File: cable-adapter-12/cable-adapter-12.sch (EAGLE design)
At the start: 40 parts

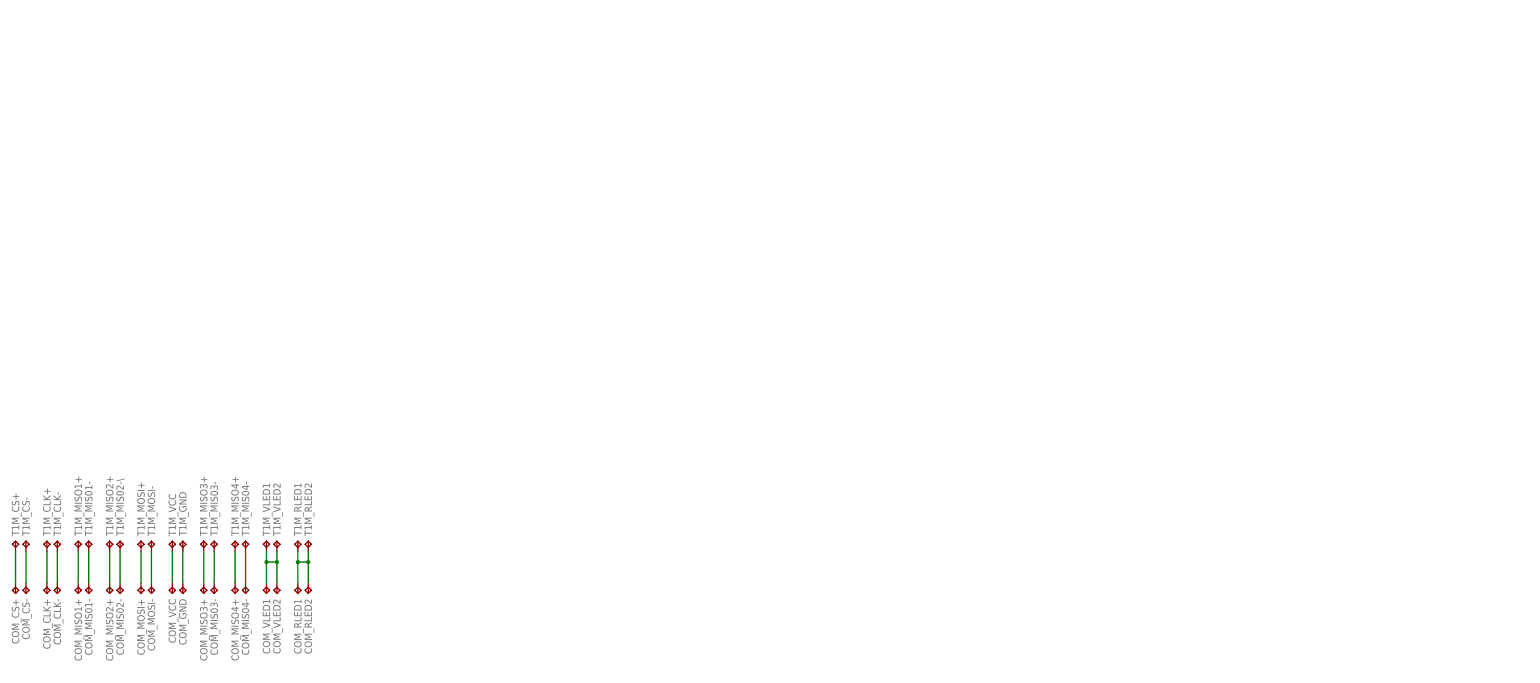
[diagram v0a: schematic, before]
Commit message: Sent three boards out for printing
- 24 circuit commutator adapter
- 12 circuit commutator adapter
- Gyro board (really just for testing before integration with SPI
  interface board)
- Need to update BOM sheet to include these guys
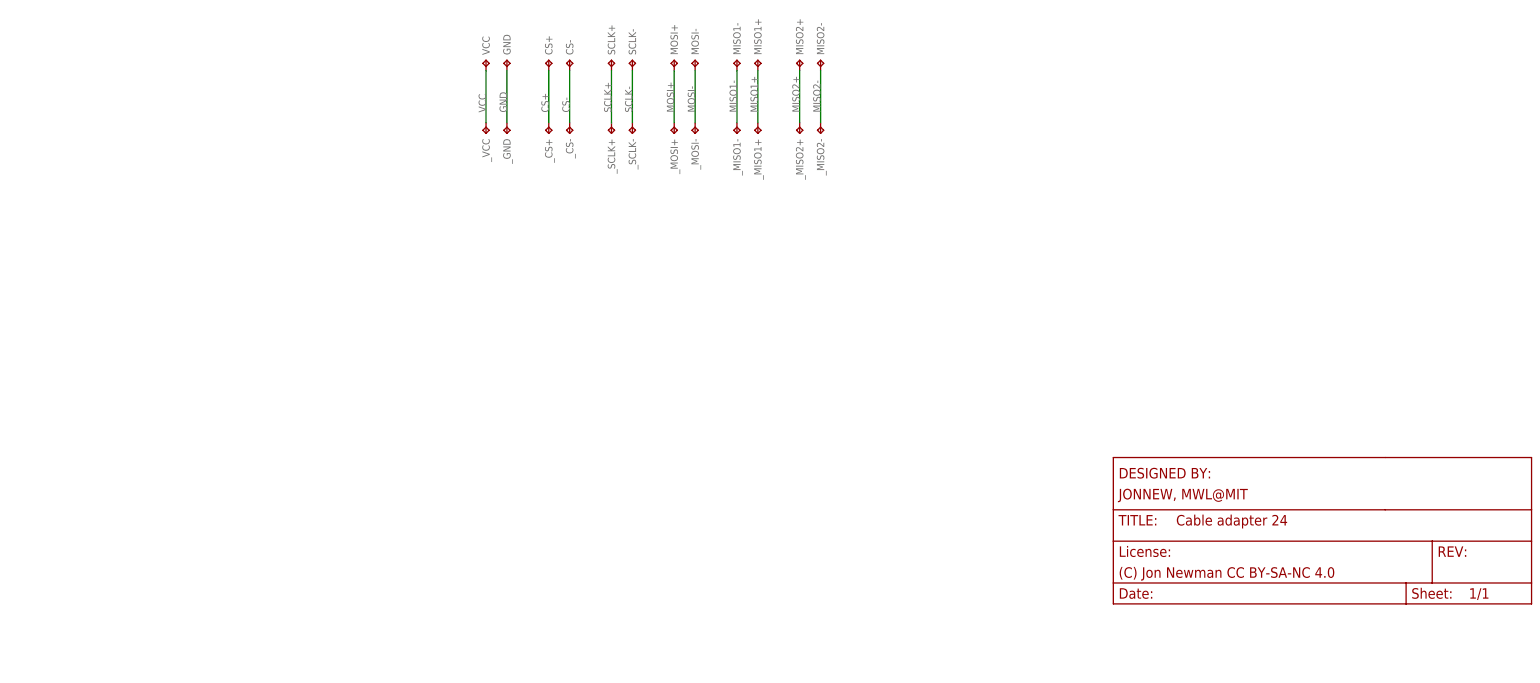
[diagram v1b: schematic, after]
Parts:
- removed COM_CLK+, COM_CLK-, COM_CS+, COM_CS-, COM_GND, COM_MIS01-, COM_MIS02-, COM_MIS03-, COM_MIS04-, COM_MISO1+, COM_MISO2+, COM_MISO4+, COM_MOSI+, COM_MOSI-, COM_RLED1, COM_RLED2, COM_VCC, COM_VLED1, COM_VLED2, T1M_CLK+, T1M_CLK-, T1M_CS+, T1M_CS-, T1M_GND, T1M_MIS01-, T1M_MIS02-\, T1M_MIS03-, T1M_MIS04-, T1M_MISO1+, T1M_MISO2+, T1M_MISO3+, T1M_MISO4+, T1M_MOSI+, T1M_MOSI-, T1M_RLED1, T1M_RLED2, T1M_VCC, T1M_VLED1, T1M_VLED2: (no value), jonnew:TP_SPI_WIRE+
- removed COM_MISO3+: MISO3+, jonnew:TP_SPI_WIRE+
- added CS+, CS-, GND, MISO1+, MISO1-, MISO2+, MISO2-, MOSI+, MOSI-, SCLK+, SCLK-, VCC, _CS+, _CS-, _GND, _MISO1+, _MISO1-, _MISO2+, _MISO2-, _MOSI+, _MOSI-, _SCLK+, _SCLK-, _VCC: (no value), jonnew:TP_SPI_WIRE+
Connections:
- removed net +LED: COM_VLED1.TP, COM_VLED2.TP, T1M_VLED1.TP, T1M_VLED2.TP
- removed net -LED: COM_RLED1.TP, COM_RLED2.TP, T1M_RLED1.TP, T1M_RLED2.TP
- removed net CLK+: COM_CLK+.TP, T1M_CLK+.TP
- removed net CLK-: COM_CLK-.TP, T1M_CLK-.TP
- removed net MIS02-: COM_MIS02-.TP, T1M_MIS02-\.TP
- removed net MIS02-1: COM_MIS04-.TP, T1M_MIS04-.TP
- removed net MISO1+1: COM_MISO3+.TP, T1M_MISO3+.TP
- removed net MISO1-1: COM_MIS03-.TP, T1M_MIS03-.TP
- removed net MISO2+1: COM_MISO4+.TP, T1M_MISO4+.TP
- new net MISO2-: MISO2-.TP, _MISO2-.TP
- new net SCLK+: SCLK+.TP, _SCLK+.TP
- new net SCLK-: SCLK-.TP, _SCLK-.TP
- net CS+: now also CS+.TP, _CS+.TP; no longer COM_CS+.TP, T1M_CS+.TP
- net CS-: now also CS-.TP, _CS-.TP; no longer COM_CS-.TP, T1M_CS-.TP
- net GND: now also GND.TP, _GND.TP; no longer COM_GND.TP, T1M_GND.TP
- net MISO1+: now also MISO1+.TP, _MISO1+.TP; no longer COM_MISO1+.TP, T1M_MISO1+.TP
- net MISO1-: now also MISO1-.TP, _MISO1-.TP; no longer COM_MIS01-.TP, T1M_MIS01-.TP
- net MISO2+: now also MISO2+.TP, _MISO2+.TP; no longer COM_MISO2+.TP, T1M_MISO2+.TP
- net MOSI+: now also MOSI+.TP, _MOSI+.TP; no longer COM_MOSI+.TP, T1M_MOSI+.TP
- net MOSI-: now also MOSI-.TP, _MOSI-.TP; no longer COM_MOSI-.TP, T1M_MOSI-.TP
- net VCC: now also VCC.TP, _VCC.TP; no longer COM_VCC.TP, T1M_VCC.TP
